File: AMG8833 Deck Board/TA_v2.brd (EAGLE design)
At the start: 55 x 32.5 mm, 18 parts, among them U2 3.3V

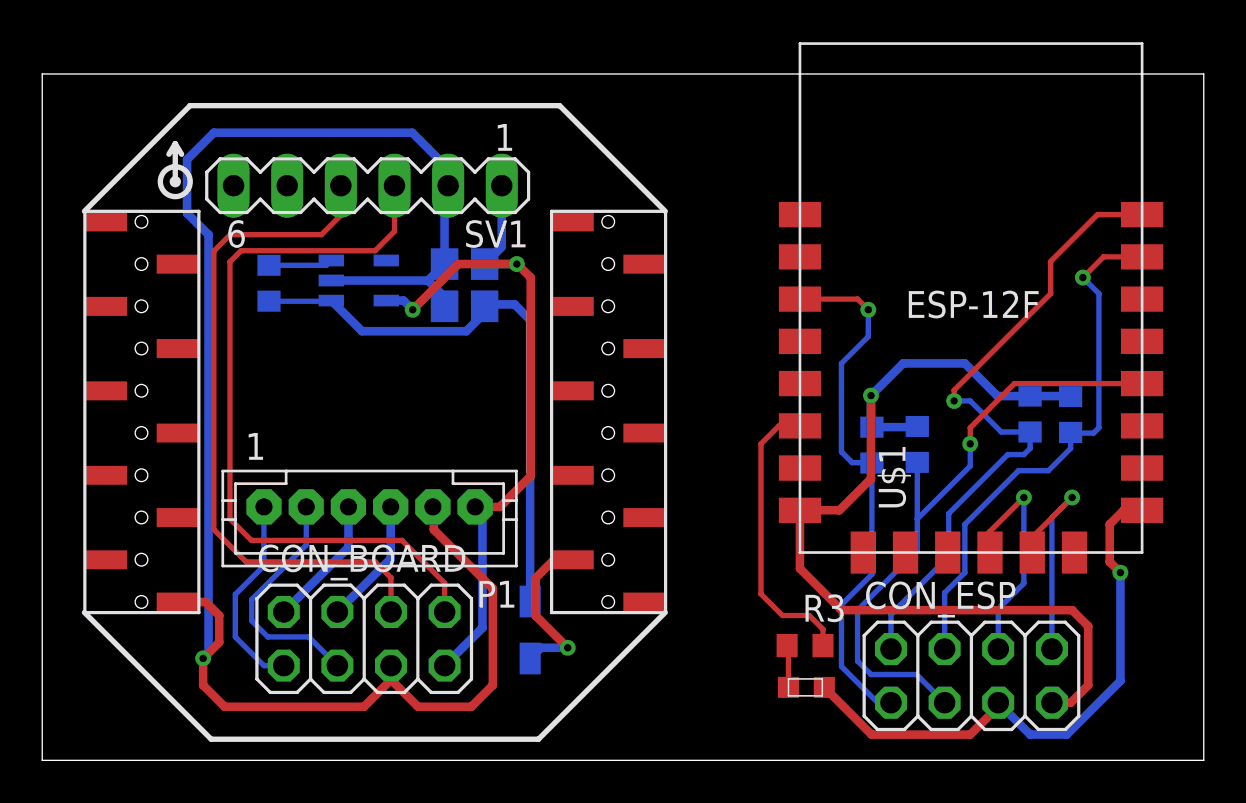
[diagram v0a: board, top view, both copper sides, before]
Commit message: Update TA_v2.brd
Update AMG8833 Deck Board design, change part placement, library update, dimension update, added milling and copper pour area
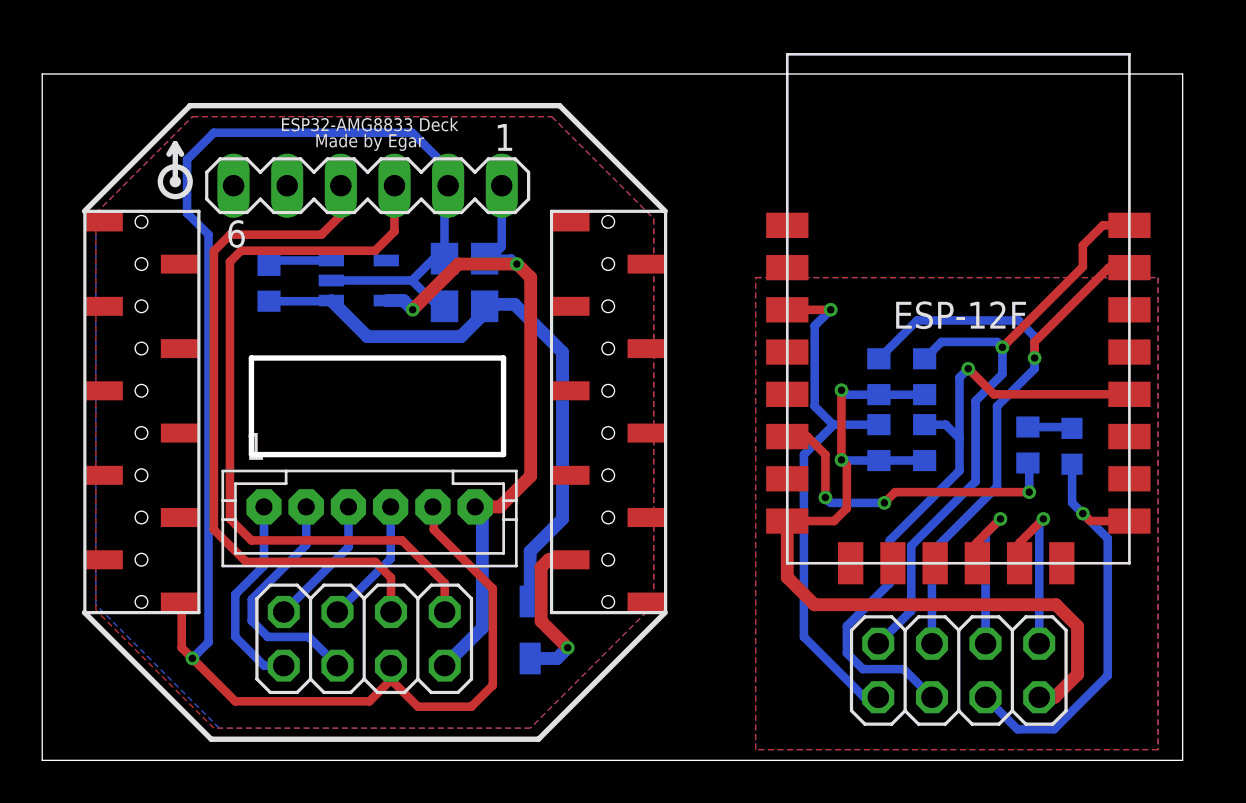
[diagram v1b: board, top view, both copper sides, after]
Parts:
- moved U$3 17.1 mm to (48.8, 14.9), flipped to the bottom, turned to 270 degrees
- moved R3 14.2 mm to (46.7, 14.9), flipped to the bottom, turned to 270 degrees
- moved R6 9.25 mm to (39.6, 18.2), turned to 270 degrees
- moved R5 5.30 mm to (41.8, 18.2), turned to 270 degrees
- moved U$1 0.79 mm to (42.9, 19.5)
- moved CON_ESP 0.65 mm to (43.4, 4.25)
- moved R2 0.36 mm to (41.8, 15.0), turned to 270 degrees
- moved R1 0.35 mm to (39.6, 15.0), turned to 270 degrees
- moved C2 0.25 mm to (20.0, 23.8)
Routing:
- net GND: track 108.2 -> 100.4 mm
- net VCC: track 79.7 -> 73.8 mm, vias 3 -> 4
- net RX: track 32.0 -> 37.7 mm
- net SDA: track 43.3 -> 41.1 mm
- net TX: track 37.7 -> 35.8 mm
- net STAT: track 13.7 -> 15.6 mm, vias 0 -> 3
- net SCL: track 46.5 -> 44.8 mm
- net N$2: track 27.3 -> 28.8 mm
- net BOOT: track 41.3 -> 42.2 mm
- added copper zone on layer 1, net GND
- added copper zone on layer 16, net GND
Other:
- board size 55 x 32.5 mm -> 54 x 32.5 mm
- board text added: "AMG8833-CONN"
- board text added: "ESP32 Breakout Board"
- board text added: "ESP32-AMG8833 Deck Made by Egar"
- board text added: "ESP32-CONN"
- board text added: "LED"
- board text added: "PROG"
